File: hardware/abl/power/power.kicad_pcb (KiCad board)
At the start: 2 copper layers, 110 x 75.9 mm, 38 parts, among them J1 Terminal_01x03, J2 Terminal_01x03, J3 009159008603906, U1 TWGMC AMS1117-3.3, U2 TMP1075D, U3 INA219AxD

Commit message: A few smaller updates to some PCBs and their READMEs.
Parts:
- D1: footprint LED_THT:LED_D3.0mm_Horizontal_O3.81mm_Z10.0mm -> Own footprints:XINGLIGHT XL-3210SURC; moved to B.Cu
- J3: footprint 009159008603906:009159008603906 -> Own footprints:Dual Row Inverted Thru Board Card Edge Connector 02x04 Kyocera AVX 009159008603906
- moved D1 1.58 mm to (144.6, 112.1)
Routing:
- net +3.3V: track 109.7 -> 109.2 mm
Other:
- board text added: "ABL Power Module V1.1"
- board text removed: "+"
- board text removed: "-"
- board text removed: "ABL Power Module V1.0"

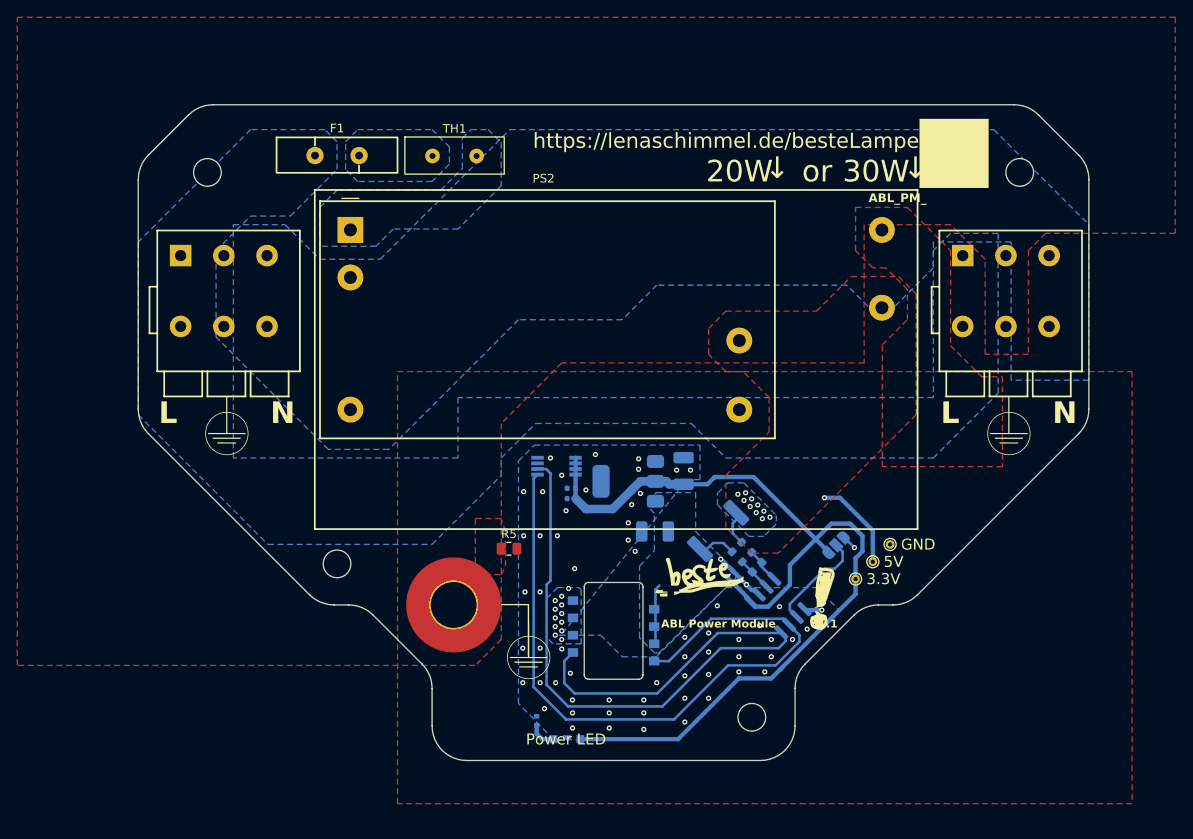
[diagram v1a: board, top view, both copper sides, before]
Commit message: Increase clearance of 230V nets to 3.175 mm, the maximum that is attainable with WAGO connerctors anyway.
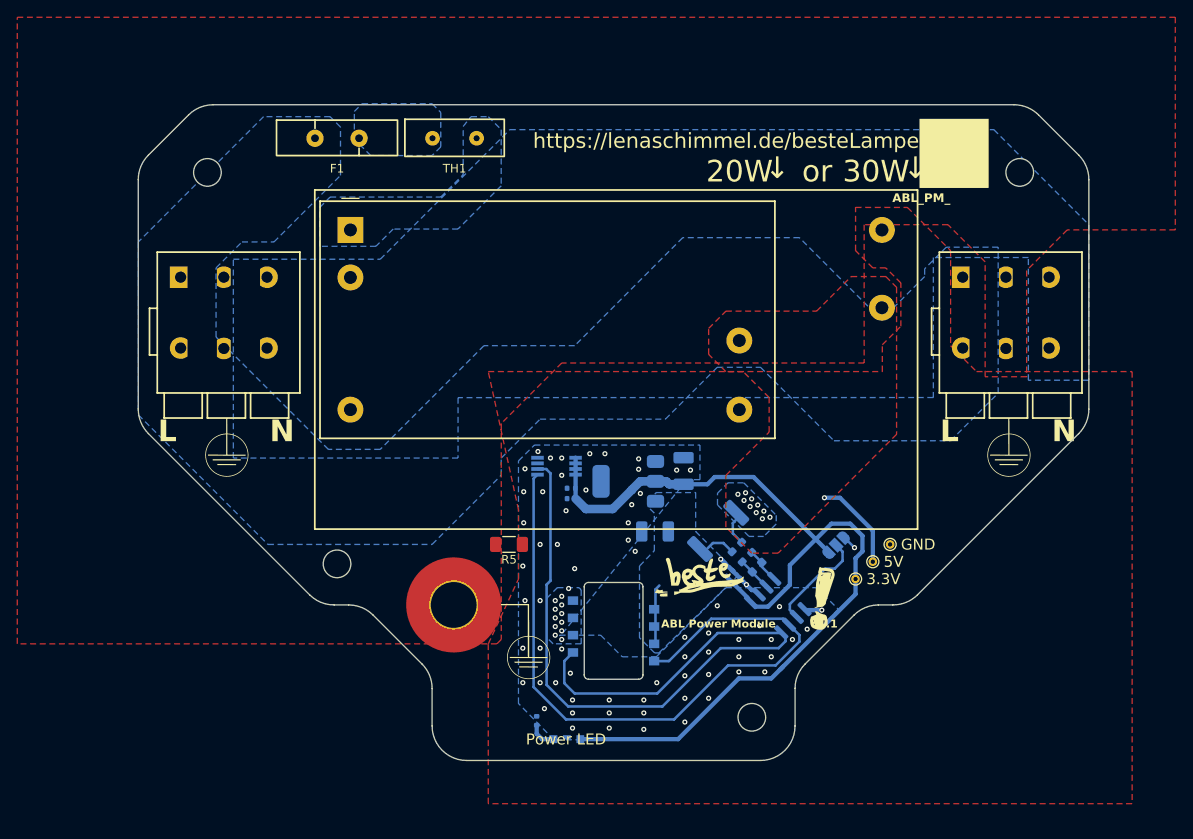
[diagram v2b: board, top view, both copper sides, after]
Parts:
- R5: footprint Resistor_SMD:R_0805_2012Metric -> Resistor_SMD:R_1206_3216Metric_Pad1.30x1.75mm_HandSolder
- moved G*** 2.50 mm to (195.8, 78.8)
- moved G*** 2.50 mm to (105.2, 78.8)
- moved J1 2.50 mm to (190.4, 59.1)
- moved J2 2.50 mm to (99.9, 59.1)
- moved TH1 2.05 mm to (131.6, 43.0)
- moved F1 2.00 mm to (118.0, 43.0)
- moved G*** 1.51 mm to (195.4, 72.5)
- moved G*** 1.50 mm to (104.9, 72.5)
- moved R5 0.50 mm to (137.9, 90.0)
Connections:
- J1 pad 2: /L -> Earth_Protective
- J1 pad 3: Earth_Protective -> /N
- J2 pad 2: /L -> Earth_Protective
- J2 pad 3: Earth_Protective -> /N
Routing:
- net GND: vias 76 -> 81

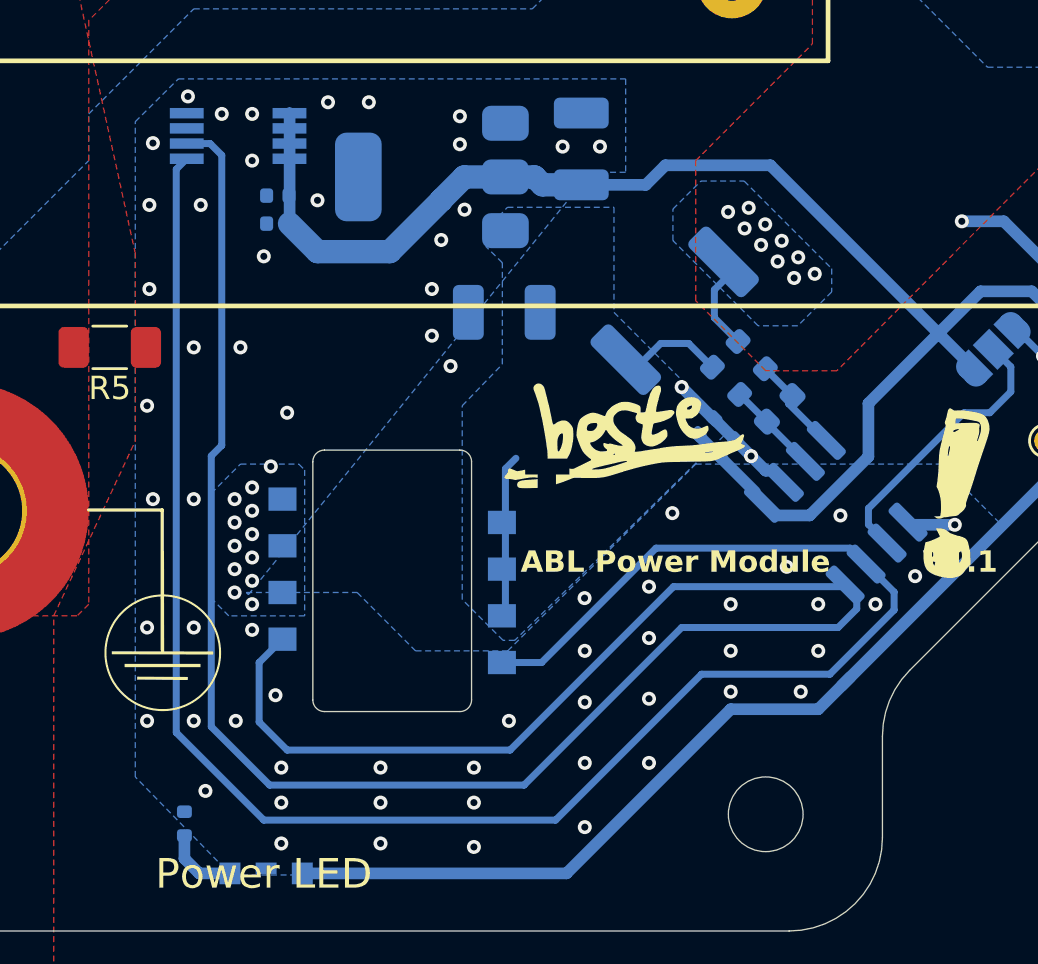
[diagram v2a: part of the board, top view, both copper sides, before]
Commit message: Added an EEPROM to the power module and changed the EEPROM on the LED module to be individually addressable.
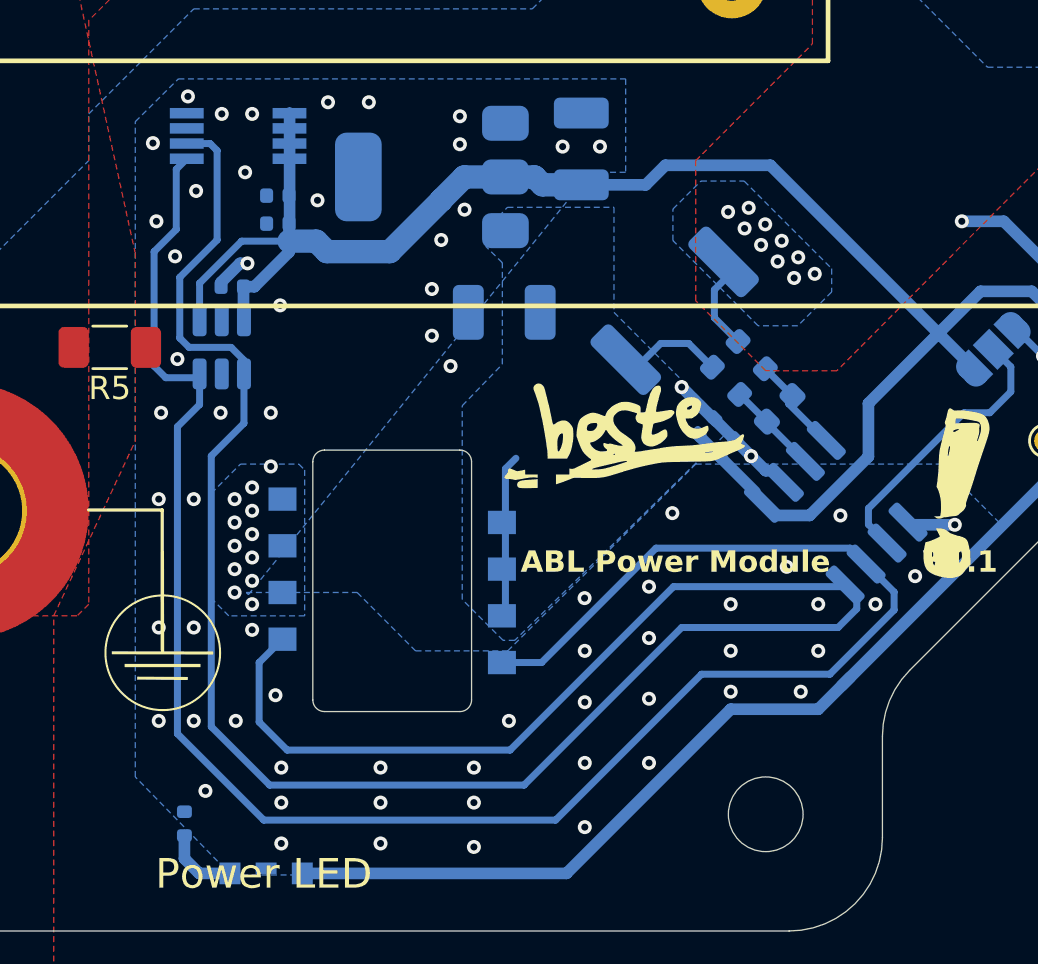
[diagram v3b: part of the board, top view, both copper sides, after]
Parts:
- added C8: 100nF, Capacitor_SMD:C_0402_1005Metric, B.Cu at (143.2, 87.4)
- added U4: 24AA025UIDT-I/OT, Package_TO_SOT_SMD:SOT-23-6, B.Cu at (142.7, 90.0)
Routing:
- net +3.3V: track 109.2 -> 120.4 mm
- net /SCL: track 91.9 -> 95.1 mm
- net /SDA: track 81.1 -> 83.7 mm
- net GND: track 9.09 -> 10.7 mm, vias 81 -> 82

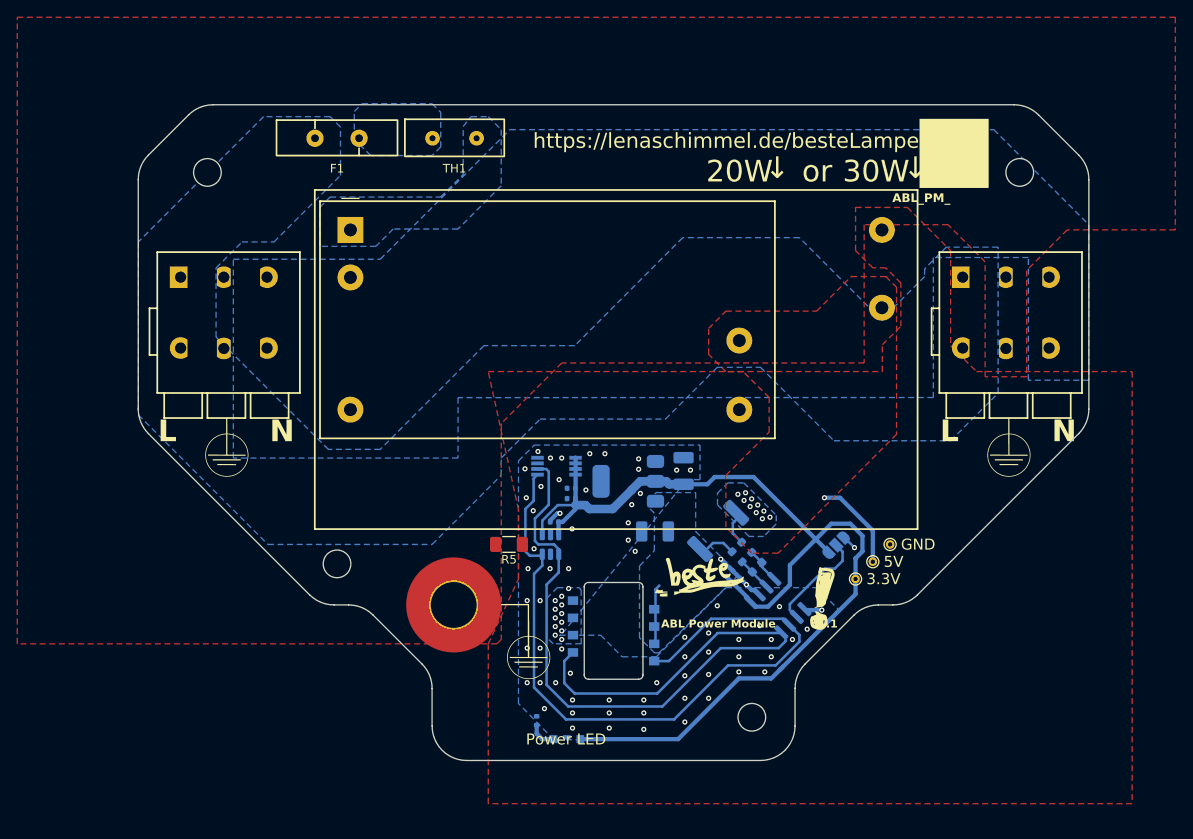
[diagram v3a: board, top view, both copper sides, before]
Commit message: Move LED and let it shine brighter, extend outline, many small enhancements.
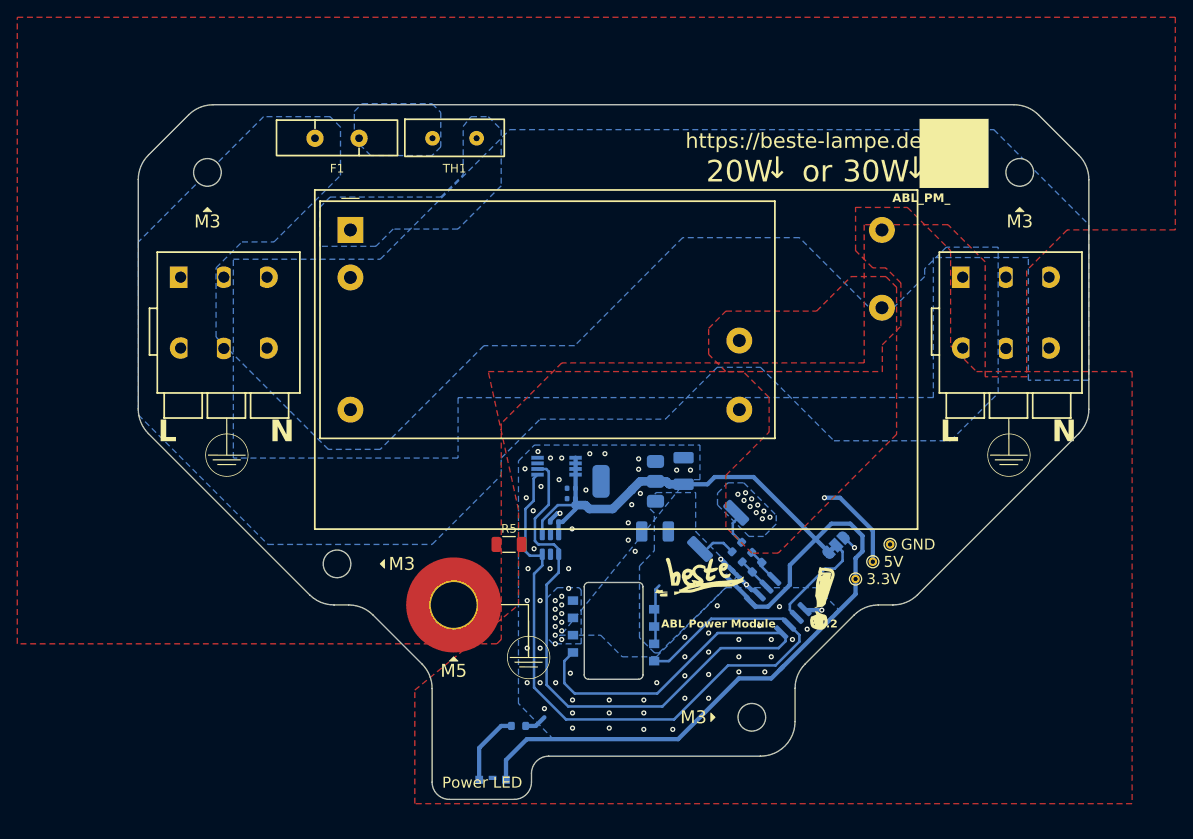
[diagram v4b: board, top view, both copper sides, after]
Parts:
- JP1: footprint Jumper:SolderJumper-3_P1.3mm_Open_RoundedPad1.0x1.5mm -> Jumper:SolderJumper-3_P1.3mm_Bridged12_RoundedPad1.0x1.5mm
- R1: value 2.2kR -> 470R; footprint Resistor_SMD:R_0402_1005Metric -> Resistor_SMD:R_0603_1608Metric
- R5: footprint Resistor_SMD:R_1206_3216Metric_Pad1.30x1.75mm_HandSolder -> Resistor_SMD:R_1206_3216Metric
- moved D1 9.80 mm to (136.0, 116.8)
- moved R1 2.18 mm to (139.0, 111.0), turned to 0 degrees
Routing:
- net +3.3V: track 120.4 -> 132.3 mm
- net Net-(D1-K): track 3.20 -> 8.46 mm
- net GND: track 10.7 -> 13.3 mm
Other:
- board size 110 x 75.9 mm -> 110 x 80.4 mm
- board text added: "+5V"
- board text added: "ABL Power Module V1.2"
- board text added: "Bridge 2 pads to indicate PS wattage (30W by default)"
- board text added: "M3"
- board text added: "M5"
- board text added: "SCL"
- board text added: "SDA"
- board text added: "https://beste-lampe.de"
- board text removed: "ABL Power Module V1.1"
- board text removed: "Always bridge 2 pads to indicate PS wattage:"
- board text removed: "https://lenaschimmel.de/besteLampe!"

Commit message: Greatly increase clearance for 230V tracks. Chosen 30W power supply and removed option for 20W. Many other small improvements.
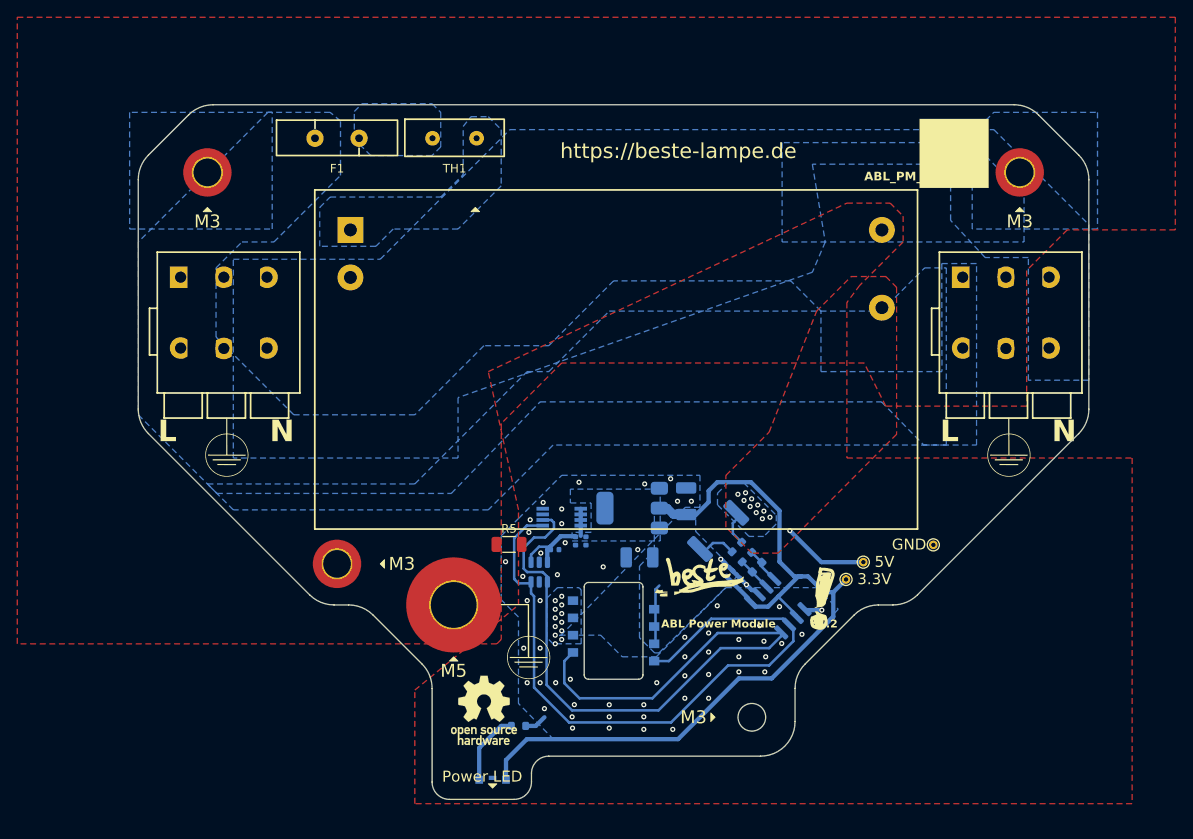
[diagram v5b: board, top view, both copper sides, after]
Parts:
- removed JP1: SolderJumper_3_Bridged12, Jumper:SolderJumper-3_P1.3mm_Bridged12_RoundedPad1.0x1.5mm
- added REF**: OSHW-Logo_7.5x8mm_SilkScreen, Symbol:OSHW-Logo_7.5x8mm_SilkScreen, F.Cu at (135.0, 109.2)
- H1, H2, H4: footprint MountingHole:MountingHole_3.2mm_M3_DIN965 -> MountingHole:MountingHole_3.2mm_M3_DIN965_Pad_TopOnly
- PS2: footprint Own footprints:Converter_ACDC_MeanWell_IRM-20+30-xx_THT_combined -> Own footprints:Converter_ACDC_MeanWell_IRM-30-xx_THT
- moved C3 6.12 mm to (145.6, 89.6), turned to 90 degrees
- moved U2 5.93 mm to (144.0, 86.8)
- moved C2 5.19 mm to (146.8, 89.6), turned to 90 degrees
- moved TP3 5.00 mm to (187.0, 90.0)
- moved C7 3.51 mm to (158.4, 85.0)
- moved C1 3.50 mm to (153.0, 91.5)
- moved U4 3.45 mm to (141.4, 93.2)
- moved C8 3.20 mm to (143.2, 90.6), turned to 180 degrees
- moved U1 3.13 mm to (152.2, 85.8)
- moved TP1 1.10 mm to (178.9, 92.0)
- moved TP2 1.10 mm to (176.9, 94.0)
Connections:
- U1 pad 4: (no net) -> +3.3V
- U3 pad 2: Net-(JP1-C) -> +3.3V
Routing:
- net +3.3V: track 132.3 -> 109.4 mm
- net Net-(JP1-C): track 12.1 -> 0.00 mm
- net /SCL: track 95.1 -> 89.9 mm
- net /SDA: track 83.7 -> 78.7 mm
- net GND: track 13.3 -> 9.97 mm, vias 82 -> 71
- net +5V: track 13.9 -> 13.1 mm
- added copper zone on B.Cu, net +3.3V
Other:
- board text removed: "20W"
- board text removed: "30W"
- board text removed: "Bridge 2 pads to indicate PS wattage (30W by default)"
- board text removed: "or"
- board text removed: "↓"
- board text removed: "≥"

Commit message: Many small adjustments for the next production run.
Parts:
- added REF**: Symbol_HighVoltage_Triangle_8x7mm_Copper, Symbol:Symbol_HighVoltage_Triangle_8x7mm_Copper, B.Cu at (150.0, 46.0)
- C8: value 100nF -> 100n
- U4: value 24AA025UIDT-I/OT -> 24AA025E48T-I/OT
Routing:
- net GND: vias 71 -> 70
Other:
- board text added: "ABL Power Module v1.2.1"
- board text added: "ST3-L6"
- board text removed: "ABL Power Module V1.2"
- board text removed: "M3"
